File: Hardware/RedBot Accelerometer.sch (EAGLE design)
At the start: 20 parts, among them U1 MMA8452QMMA8452Q-1:1, U2 MIC5205-3.3V, U3 PCA9306

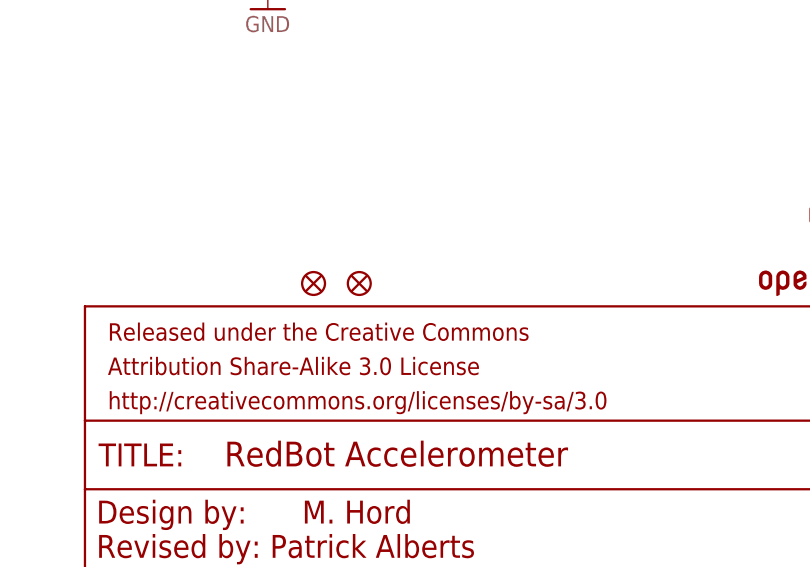
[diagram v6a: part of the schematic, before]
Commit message: changed fids from micro to regular
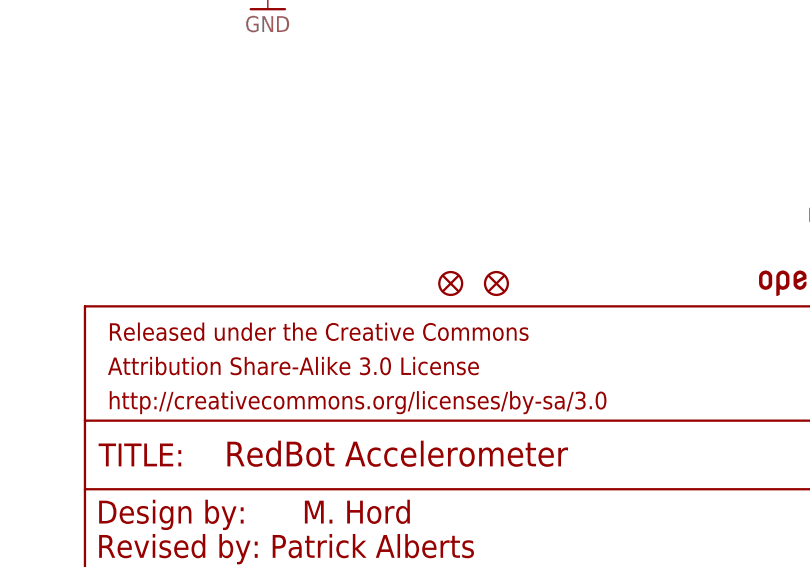
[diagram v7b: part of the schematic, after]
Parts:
- removed FID2: FIDUCIALUFIDUCIAL, SparkFun-Aesthetics:FIDUCIALUFIDUCIAL
- added FID3: FIDUCIAL1X2, SparkFun-Aesthetics:FIDUCIAL1X2
- FID1: value FIDUCIALUFIDUCIAL -> FIDUCIAL1X2; device SparkFun-Aesthetics:FIDUCIALUFIDUCIAL -> SparkFun-Aesthetics:FIDUCIAL1X2
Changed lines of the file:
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@@
 <part name="GND6" library="SparkFun-Aesthetics" deviceset="GND" device=""/>
 <part name="SUPPLY8" library="SparkFun-Aesthetics" deviceset="5V" device=""/>
-<part name="FID1" library="SparkFun-Aesthetics" deviceset="FIDUCIAL" device="UFIDUCIAL"/>
-<part name="FID2" library="SparkFun-Aesthetics" deviceset="FIDUCIAL" device="UFIDUCIAL"/>
+<part name="FID3" library="SparkFun-Aesthetics" deviceset="FIDUCIAL" device="1X2"/>
+<part name="FID1" library="SparkFun-Aesthetics" deviceset="FIDUCIAL" device="1X2"/>
 </parts>
 <sheets>
@@
 <instance part="GND6" gate="1" x="210.82" y="111.76"/>
 <instance part="SUPPLY8" gate="G$1" x="210.82" y="137.16"/>
-<instance part="FID1" gate="G$1" x="172.72" y="38.1"/>
-<instance part="FID2" gate="G$1" x="177.8" y="38.1"/>
+<instance part="FID3" gate="G$1" x="193.04" y="38.1"/>
+<instance part="FID1" gate="G$1" x="187.96" y="38.1"/>
 </instances>
 <busses>

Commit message: pushing v14
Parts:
- removed C4: 0.1uF, SparkFun-Capacitors:0.1UF-25V(+80/-20%)(0603)
- removed R2, R3, R4, R5: 1k, SparkFun-Resistors:1K-1%
- removed R6: 200k, SparkFun-Resistors:200KOHM1/10W1%(0603)200K
- removed U3: PCA9306, SparkFun-DigitalIC:PCA9306PCA9306DC-1:1
- added I2C: JUMPER-SMT_3_2-NC_TRACE_SILK, SparkFun-Jumpers:JUMPER-SMT_3_2-NC_TRACE_SILK
- added Q1, Q2: 220mA/50V/3.5Ω, SparkFun-DiscreteSemi:MOSFET-NCH-BSS138
- added R10, R7, R8, R9: 10k, SparkFun-Resistors:10KOHM-0603-1/10W-1%
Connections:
- removed net N$2: C4.1, R6.1, U3.EN, U3.VREF2
- removed net SCL1: R3.1, U1.SCL, U3.SCL1
- removed net SDA1: R2.1, U1.SDA, U3.SDA1
- new net LSCL: Q2.S, R9.1, U1.SCL
- new net LSDA: Q1.S, R8.1, U1.SDA
- new net N$3: I2C.3, R7.2
- new net N$4: I2C.1, R10.2
- net 3.3V: now also Q1.G, Q2.G, R8.2, R9.2; no longer R2.2, R3.2, U3.VREF1
- net 5V: now also I2C.2; no longer R4.2, R5.2, R6.2
- net GND: no longer C4.2, U3.GND
- net SCL: now also Q2.D, R10.1; no longer R5.1, U3.SCL2
- net SDA: now also Q1.D, R7.1; no longer R4.1, U3.SDA2
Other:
- note added: "5V -> 3.3V Conversion"
- note added: "Cut I2C Jumper to remove pullup resistors from the I2C bus"
- note added: "I2C Connections"
- note added: "MMA8452Q Accelerometer"
- note added: "Revised by: Patrick Alberts, Andy England"
- note added: "v14"
- note removed: "Revised by: Patrick Alberts"
- note removed: "v12"
- moved on the sheet: C1, C2, C3, JP1, JP2, R1, U1, U2
